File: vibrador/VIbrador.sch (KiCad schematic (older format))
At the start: 8 parts, among them U1 Pila3,7V, U2 StepDown, U3 Buzzer, U4 HC-05, U5 Buzzer, U6 PiZeroW, U7 Pila3,7V-Modulos-VIbrador-res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

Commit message: Se guardo el  PCB finallizado
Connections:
- net Rx_Rasp is gone; now on net Rx_rasp: A1.6 (D3)
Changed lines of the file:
@@
 Tx_rasp
 Text GLabel 2350 2200 0    50   Input ~ 0
-Rx_Rasp
+Rx_rasp
 Text GLabel 3850 4650 2    50   Input ~ 0
 Tx_rasp

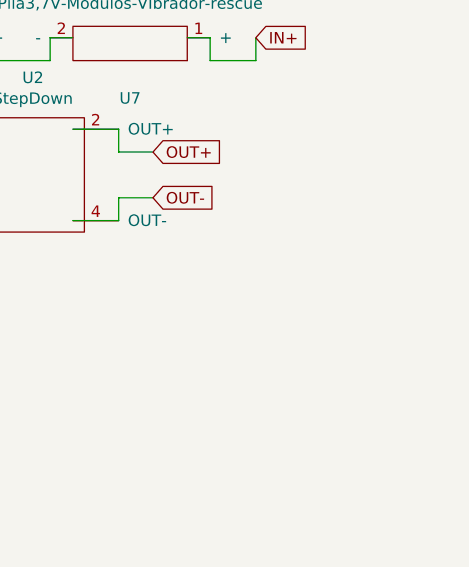
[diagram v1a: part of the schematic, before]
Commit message: Se unieron IN- Y OUT- ya que los dos son GND de el step down y es lo mismo
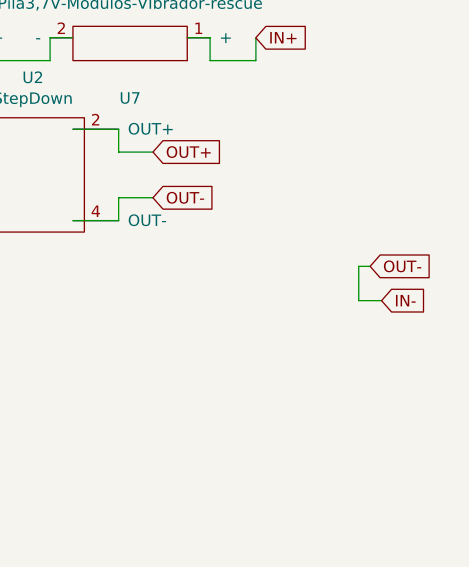
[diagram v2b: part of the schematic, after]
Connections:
- net OUT- is gone; now on net IN-: A1.29 (GND), A1.4 (GND), U2.4 (OUT-), U3.2 (GND), U4.3 (GND), U5.2 (GND), U6.20 (GND)
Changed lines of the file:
@@
 EESchema Schematic File Version 4
-LIBS:VIbrador-cache
-EELAYER 29 0
+EELAYER 30 0
 EELAYER END
 $Descr A4 8268 11693 portrait
@@
 Text GLabel 2750 1350 2    50   Input ~ 0
 OUT+
+Text GLabel 6750 3350 2    50   Input ~ 0
+OUT-
+Text GLabel 6800 3500 2    50   Input ~ 0
+IN-
+Wire Wire Line
+	6800 3500 6700 3500
+Wire Wire Line
+	6700 3500 6700 3350
+Wire Wire Line
+	6700 3350 6750 3350
 $EndSCHEMATC
